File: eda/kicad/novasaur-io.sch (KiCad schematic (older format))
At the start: 77 parts, among them J1 POWER IN, J10 EXPANSION, J11 EXPANSION, J3 AUDIO OUT, J4 KEYBOARD, J5 SERIAL, J5 VIDEO, J6 DISPLAY, J7 AUDIO, J8 EXPANSION, J9 EXPANSION, Q1 2N3904, Q2 2N3904, Q3 2N3904, SW1 POWER, SW2 RESET, U1 74F86, U3 74F11, U38 CD4053, U39 MAX232, U4 74F32, U40 NJM4580, U41 MCP1827S, U42 MCP1700, U6 74F139, U7 74F139

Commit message: add TVS diode ESD protection
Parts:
- removed J7: AUDIO, Connector_PinHeader_2.54mm:PinHeader_1x02_P2.54mm_Vertical, symbol Connector_Generic:Conn_01x02
- added D4, D5, D6: P4KE6.8CA, Diode_THT:D_DO-41_SOD81_P7.62mm_Horizontal, symbol Device:D_TVS_ALT
- C11, C12: value 22u -> 10u
- J3: footprint Connector_Audio:Jack_3.5mm_CUI_SJ1-3533NG_Horizontal -> Connector_Audio:Jack_3.5mm_CUI_SJ1-3533NG_Horizontal_CircularHoles
- J5: value VIDEO -> GPU OUT; footprint Connector_PinHeader_2.54mm:PinHeader_1x06_P2.54mm_Vertical -> Connector_PinSocket_2.54mm:PinSocket_1x08_P2.54mm_Vertical; symbol Connector_Generic:Conn_01x06 -> Connector_Generic:Conn_01x08
- renumbered J11 to J10, J8 to J7, J9 to J8, J10 to J9
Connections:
- net labels added: audio, pwron
- wire segments 332 -> 344
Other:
- moved on the sheet: J10, J4, J7, J8, J9, JP3, R10, R11, R12, R13, R14, R8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

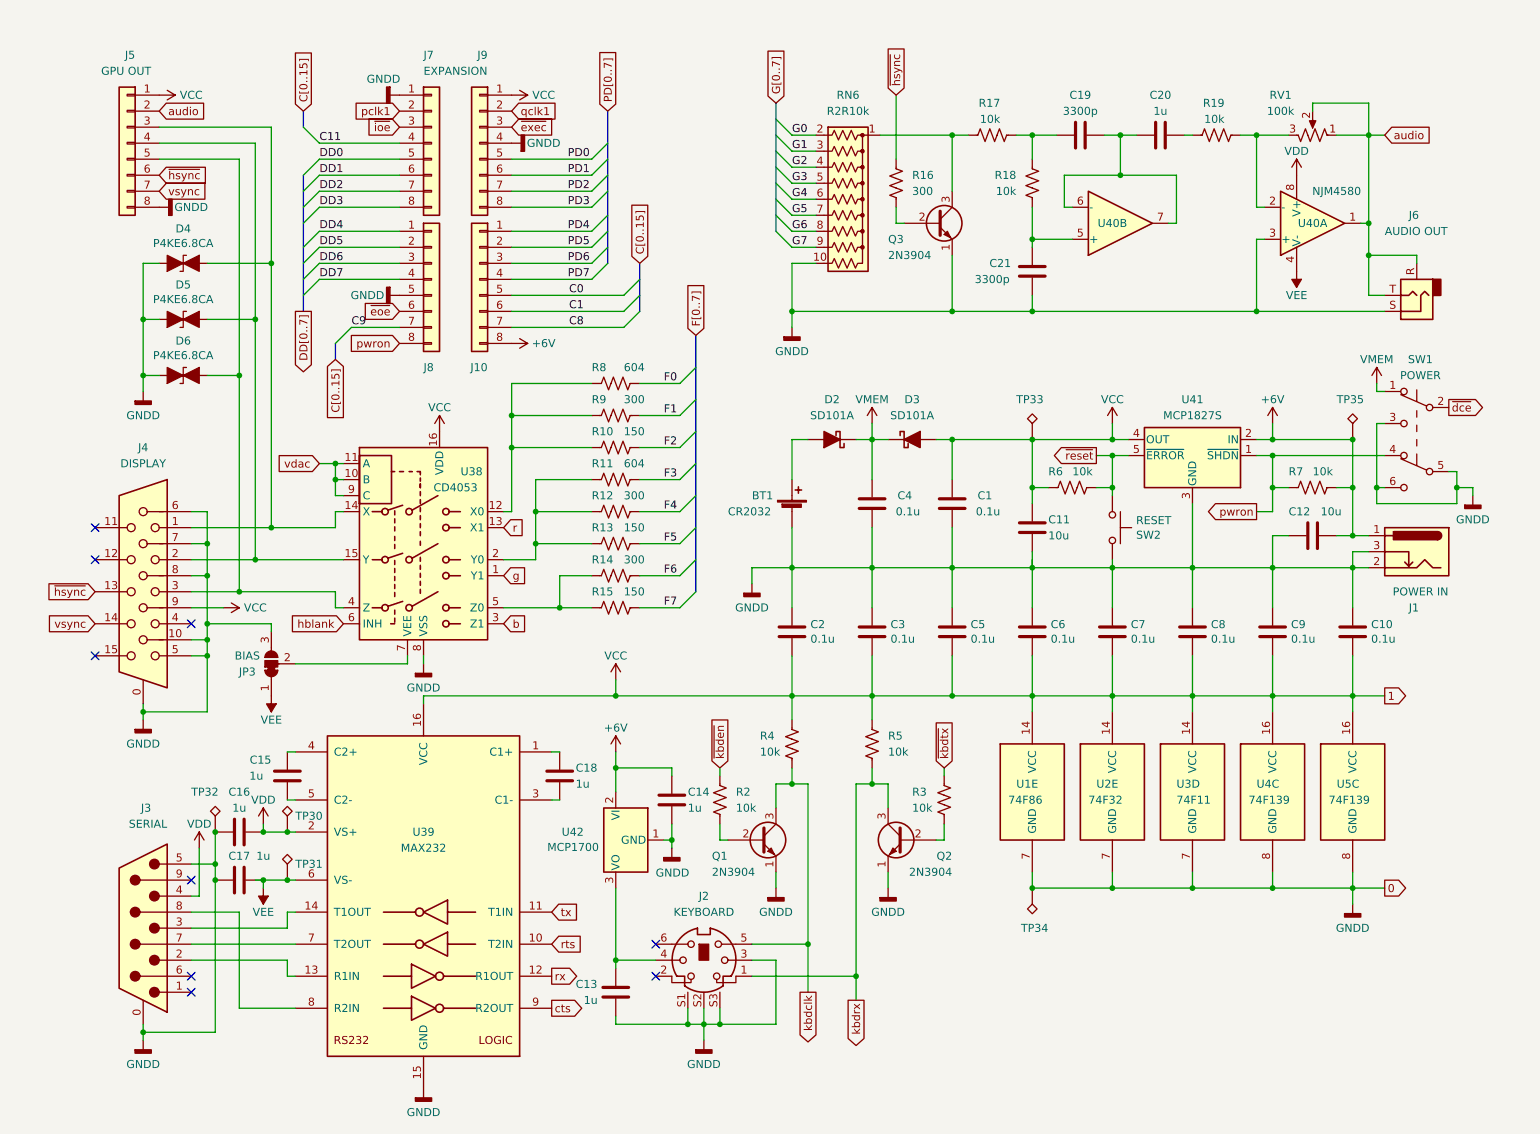
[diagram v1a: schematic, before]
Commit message: remove 6v regulator go back to rev.1 do not collect 00
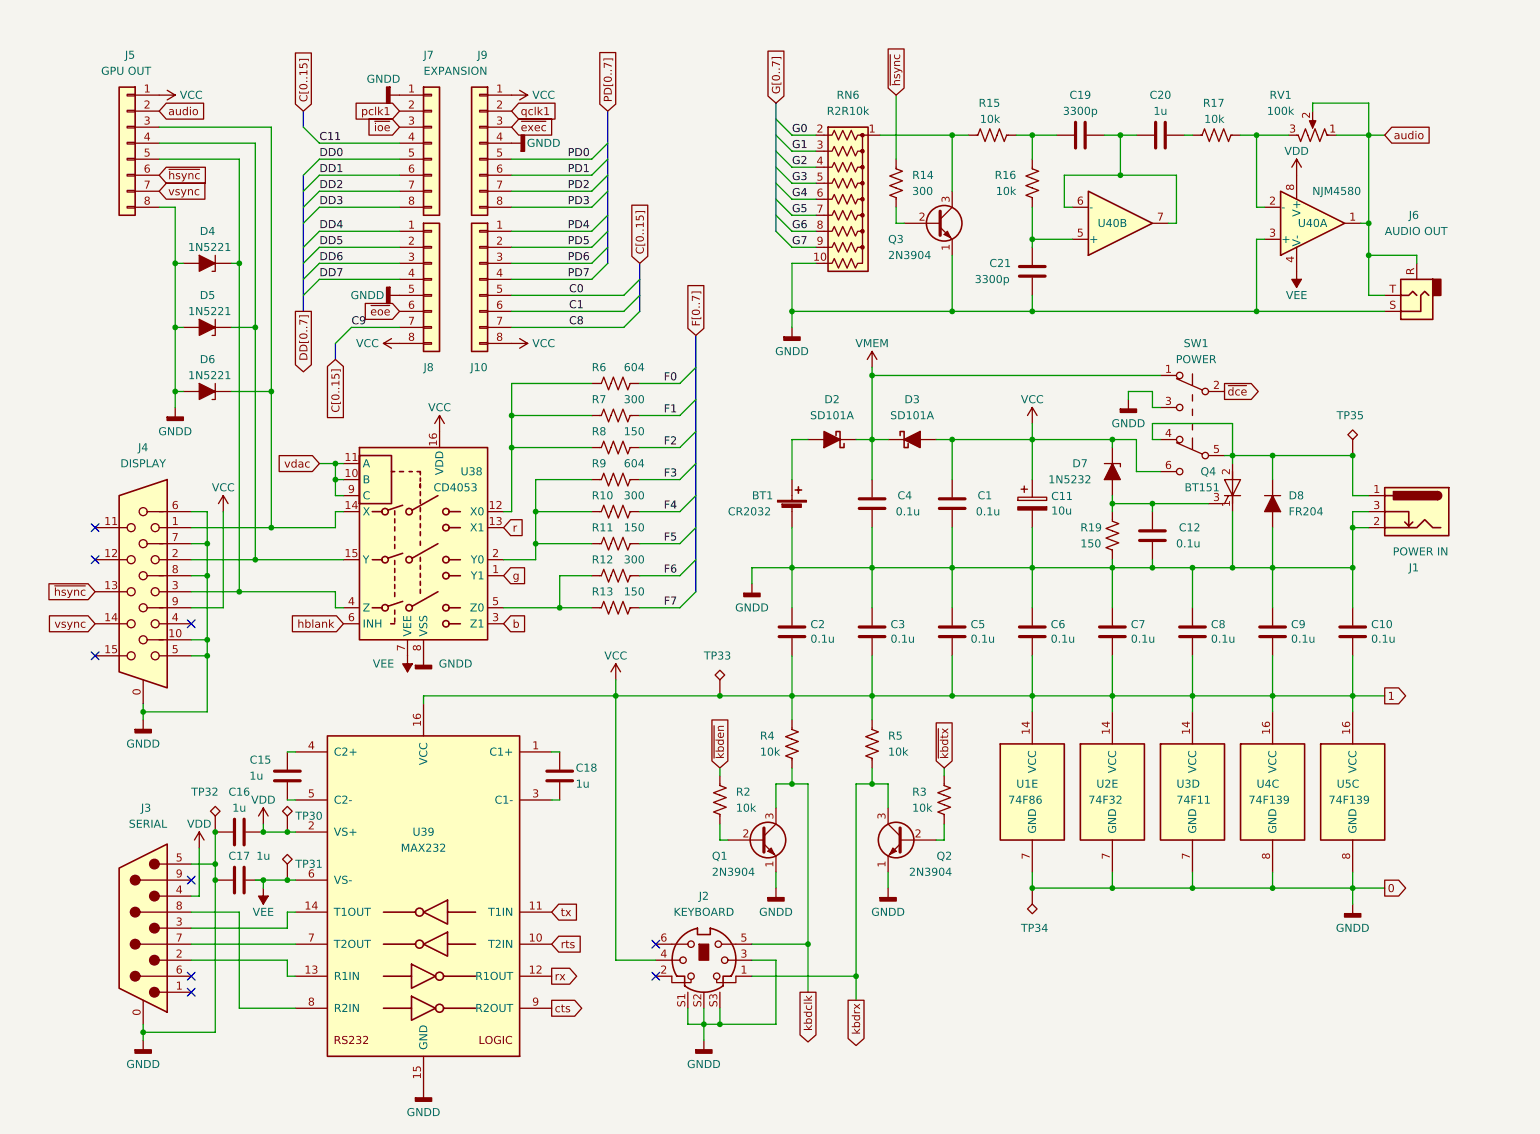
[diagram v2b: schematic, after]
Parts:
- removed C11: 10u, Capacitor_THT:C_Disc_D5.0mm_W2.5mm_P2.50mm, symbol Device:C
- removed C13, C14: 1u, Capacitor_THT:C_Disc_D5.1mm_W3.2mm_P5.00mm, symbol Device:C
- removed D4, D5, D6: P4KE6.8CA, Diode_THT:D_DO-41_SOD81_P7.62mm_Horizontal, symbol Device:D_TVS_ALT
- removed JP3: BIAS, Jumper:SolderJumper-3_P1.3mm_Bridged12_RoundedPad1.0x1.5mm, symbol Jumper:SolderJumper_3_Bridged12
- removed R6, R7: 10k, Resistor_THT:R_Axial_DIN0204_L3.6mm_D1.6mm_P7.62mm_Horizontal, symbol Device:R_US
- removed SW2: RESET, Button_Switch_THT:SW_DIP_SPSTx01_Slide_6.7x4.1mm_W7.62mm_P2.54mm_LowProfile, symbol Switch:SW_Push
- removed U41: MCP1827S, Package_TO_SOT_THT:TO-220-5_P3.4x3.8mm_StaggerOdd_Lead7.13mm_TabDown, symbol Regulator_Linear:LP3963-3.3
- removed U42: MCP1700, Package_TO_SOT_THT:TO-92_HandSolder, symbol Regulator_Linear:MCP1700-5002E_TO92
- added C11: 10u, Capacitor_THT:CP_Radial_Tantal_D5.0mm_P5.00mm, symbol Device:CP
- added D4, D5, D6: 1N5221, Diode_THT:D_DO-35_SOD27_P7.62mm_Horizontal, symbol Device:D_Zener_ALT
- added D7: 1N5232, Diode_THT:D_DO-35_SOD27_P7.62mm_Horizontal, symbol Device:D_Zener_ALT
- added D8: FR204, Diode_THT:D_DO-15_P10.16mm_Horizontal, symbol Device:D_ALT
- added Q4: BT151, Package_TO_SOT_THT:TO-220-3_Vertical, symbol Triac_Thyristor:TIC106
- added R19: 150, Resistor_THT:R_Axial_DIN0204_L3.6mm_D1.6mm_P7.62mm_Horizontal, symbol Device:R_US
- C12: value 10u -> 0.1u; footprint Capacitor_THT:C_Disc_D5.0mm_W2.5mm_P2.50mm -> Capacitor_THT:C_Disc_D5.0mm_W2.5mm_P5.00mm
- TP35: value +6v -> Vin
- renumbered R12 to R10, R13 to R11, R14 to R12, R15 to R13, R16 to R14, R17 to R15, R18 to R16, R19 to R17, R8 to R6, R9 to R7, R10 to R8, R11 to R9
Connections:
- net GNDD: now also C12.1, C11.2, D4.2 (A), D5.2 (A), D6.2 (A), D8.2 (A), Q4.1 (K), R19.2; no longer C12.2, SW1.5 (B), SW1.6 (C)
- net VCC: now also J10.8 (Pin_8), J4.4, J8.8 (Pin_8), SW1.6 (C), C11.1, D7.1 (K)
- net VEE: now also U38.7 (VEE)
- net at J5.3 (Pin_3), J6.1, U38.14 (X): now also D6.1 (K)
- net at J5.4 (Pin_4), J6.2, U38.15 (Y): now also D5.1 (K)
- net at J5.5 (Pin_5), J6.3, U38.4 (Z): now also D4.1 (K)
- net +6V: no longer names the net of J1.1, TP35.1
- net +6V: now also SW1.4 (A), SW1.5 (B), D8.1 (K), Q4.2 (A); no longer C12.1, J10.8 (Pin_8)
- removed net pwron: J8.8 (Pin_8), SW1.4 (A)
- new net: C12.2, D7.2 (A), Q4.3 (G), R19.1
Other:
- moved on the sheet: J1, SW1, TP33, TP35

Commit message: Rev. 10 with 5v PSU
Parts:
- removed D4, D5, D6: 1N5221, Diode_THT:D_DO-35_SOD27_P7.62mm_Horizontal, symbol Device:D_Zener_ALT
- added D4, D5, D6, D7, D8, D9: SD101A, Diode_THT:D_DO-35_SOD27_P7.62mm_Horizontal, symbol Device:D_Schottky_ALT
- C11: value 10u -> 22u
- D11: renamed from D8; footprint Diode_THT:D_DO-15_P10.16mm_Horizontal -> Diode_THT:D_DO-15_P12.70mm_Horizontal
- renumbered D7 to D10
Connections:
- net GNDD: now also J10.8 (Pin_8), D4.2 (A), D5.2 (A), D6.2 (A)
- net VCC: now also D7.1 (K), D8.1 (K), D9.1 (K); no longer J10.8 (Pin_8)
- net at J5.3 (Pin_3), J6.1, U38.14 (X): now also D6.1 (K), D9.2 (A)
- net at J5.4 (Pin_4), J6.2, U38.15 (Y): now also D5.1 (K), D8.2 (A)
- net at J5.5 (Pin_5), J6.3, U38.4 (Z): now also D4.1 (K), D7.2 (A)
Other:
- moved on the sheet: D11, TP34

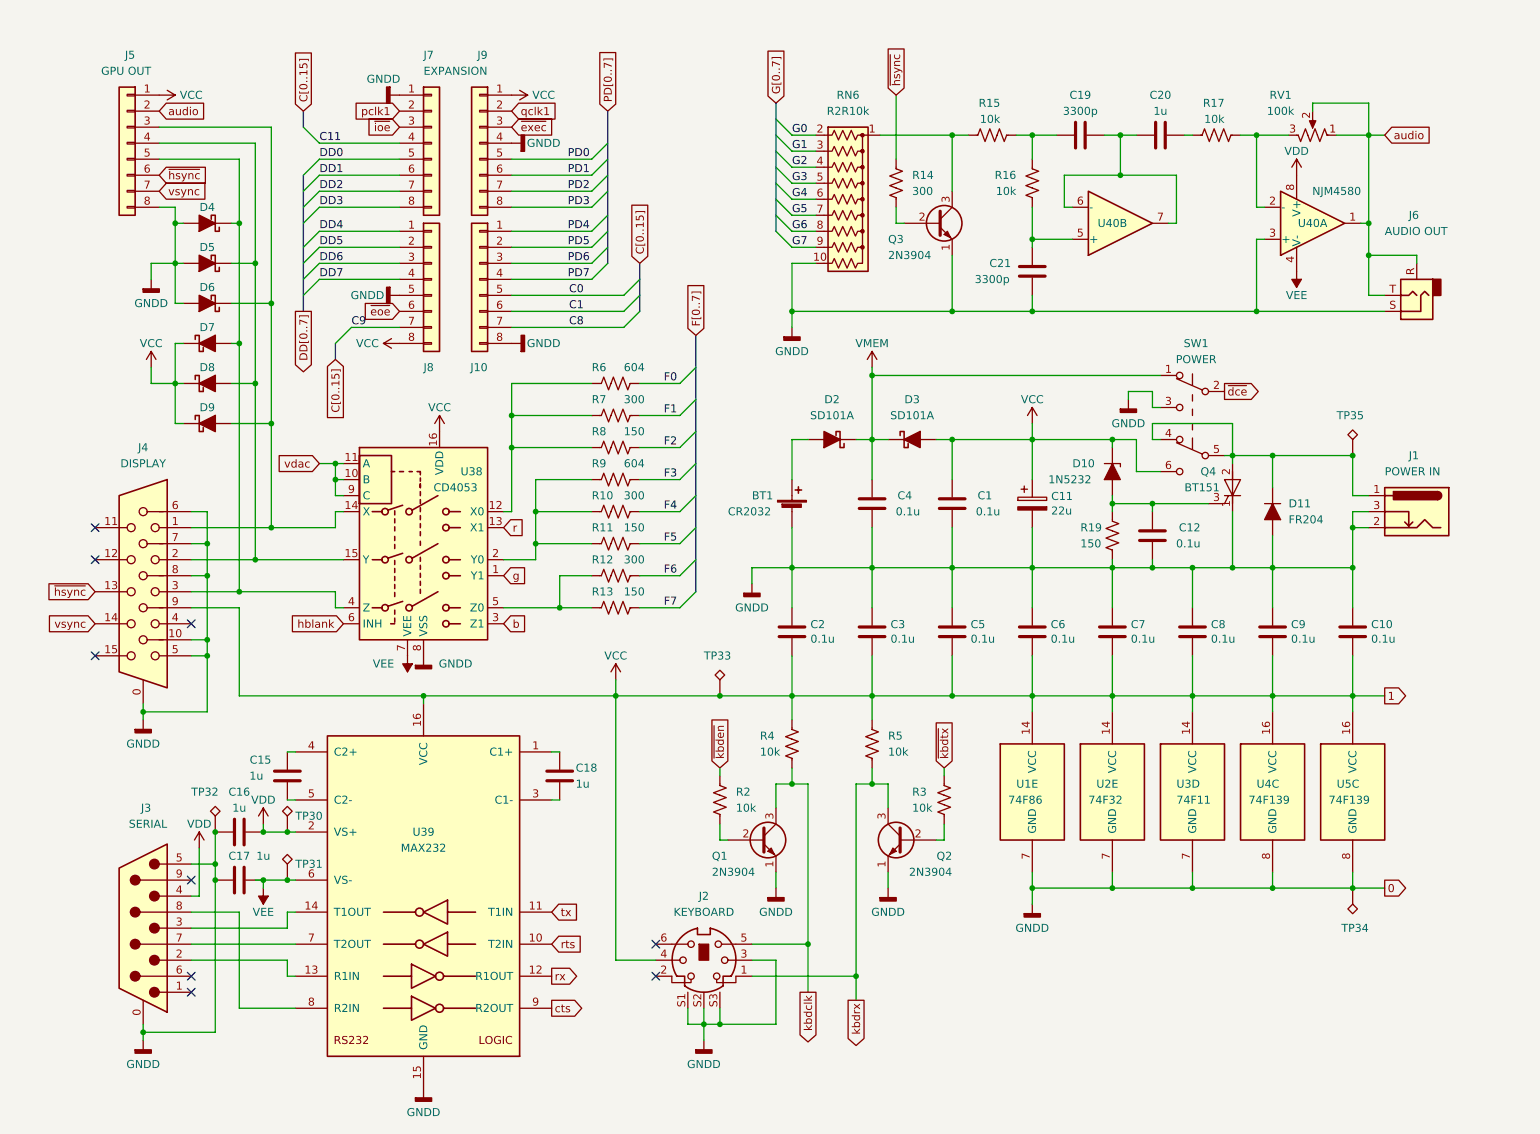
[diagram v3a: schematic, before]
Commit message: remove option for 128k RAM
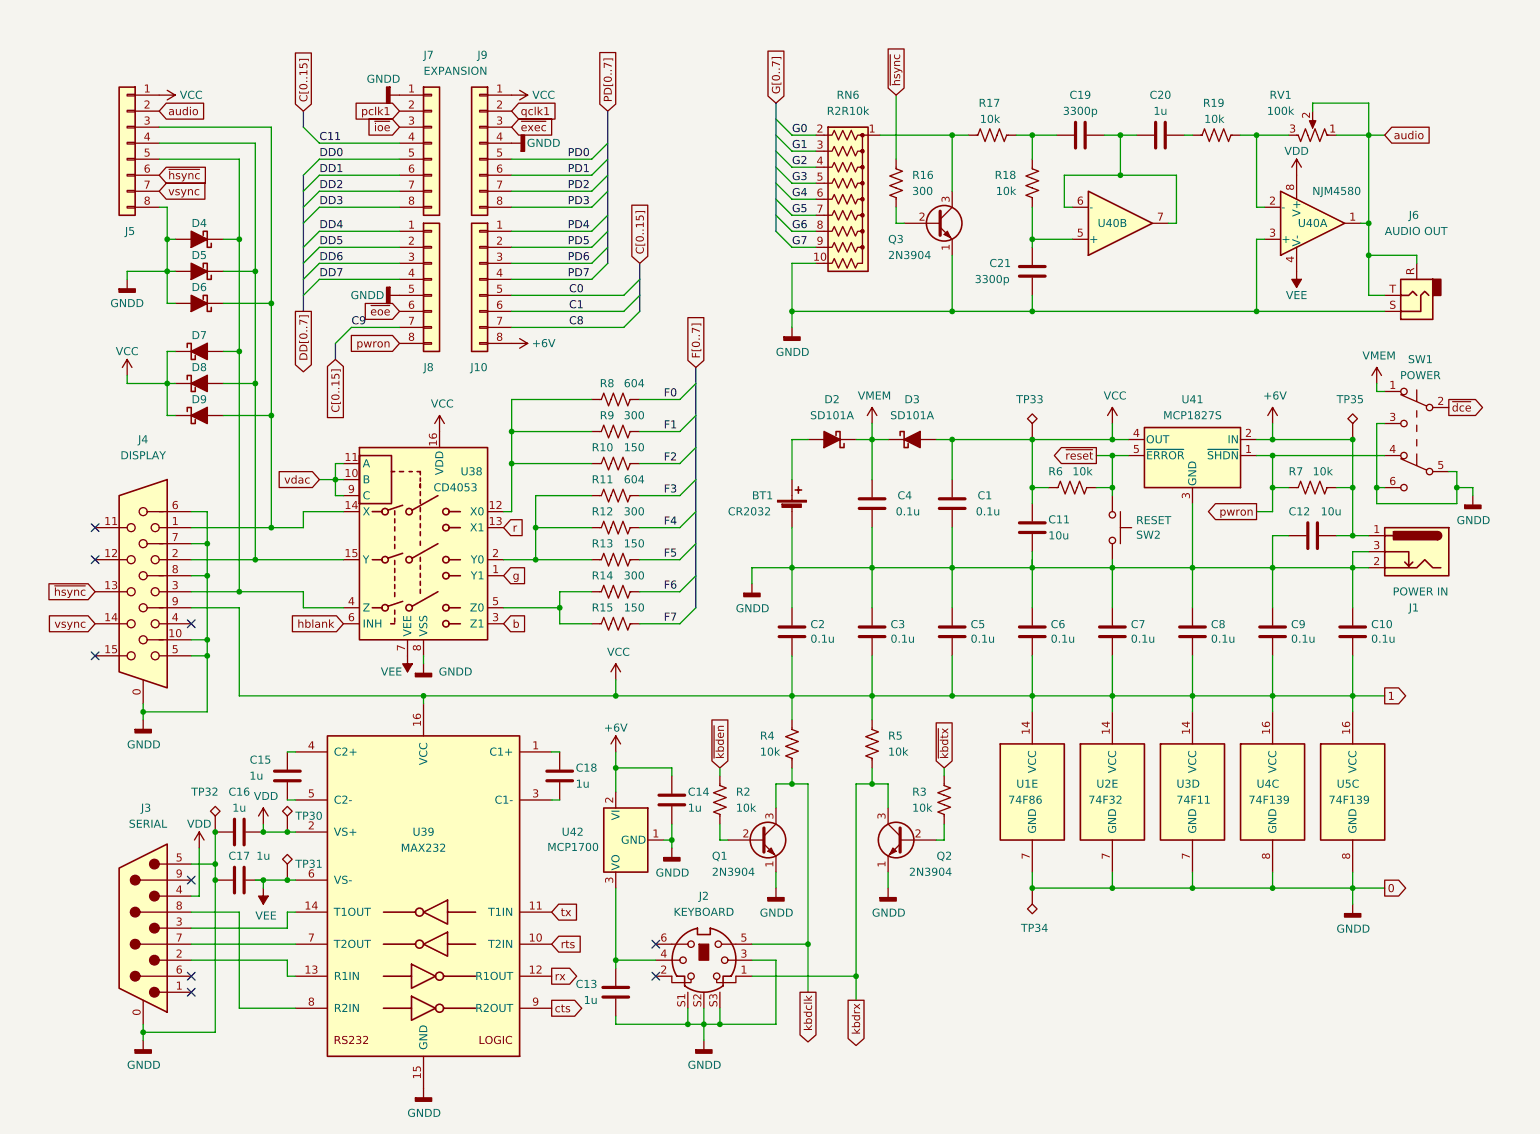
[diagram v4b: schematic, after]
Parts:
- removed C11: 22u, Capacitor_THT:CP_Radial_Tantal_D5.0mm_P5.00mm, symbol Device:CP
- removed D10: 1N5232, Diode_THT:D_DO-35_SOD27_P7.62mm_Horizontal, symbol Device:D_Zener_ALT
- removed D11: FR204, Diode_THT:D_DO-15_P12.70mm_Horizontal, symbol Device:D_ALT
- removed Q4: BT151, Package_TO_SOT_THT:TO-220-3_Vertical, symbol Triac_Thyristor:TIC106
- removed R19: 150, Resistor_THT:R_Axial_DIN0204_L3.6mm_D1.6mm_P7.62mm_Horizontal, symbol Device:R_US
- added C11: 10u, Capacitor_THT:C_Disc_D5.0mm_W2.5mm_P2.50mm, symbol Device:C
- added C13, C14: 1u, Capacitor_THT:C_Disc_D5.1mm_W3.2mm_P5.00mm, symbol Device:C
- added R6, R7: 10k, Resistor_THT:R_Axial_DIN0204_L3.6mm_D1.6mm_P7.62mm_Horizontal, symbol Device:R_US
- added SW2: RESET, Button_Switch_THT:SW_DIP_SPSTx01_Slide_6.7x4.1mm_W7.62mm_P2.54mm_LowProfile, symbol Switch:SW_Push
- added U41: MCP1827S, Package_TO_SOT_THT:TO-220-5_P3.4x3.8mm_StaggerOdd_Lead7.13mm_TabDown, symbol Regulator_Linear:LP3963-3.3
- added U42: MCP1700, Package_TO_SOT_THT:TO-92_HandSolder, symbol Regulator_Linear:MCP1700-5002E_TO92
- C12: value 0.1u -> 10u; footprint Capacitor_THT:C_Disc_D5.0mm_W2.5mm_P5.00mm -> Capacitor_THT:C_Disc_D5.0mm_W2.5mm_P2.50mm
- TP35: value Vin -> +6v
- renumbered R8 to R10, R9 to R11, R10 to R12, R11 to R13, R12 to R14, R13 to R15, R14 to R16, R15 to R17, R16 to R18, R17 to R19, R6 to R8, R7 to R9
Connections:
- net GNDD: now also C12.2, SW1.5 (B), SW1.6 (C), C11.2, C13.2, C14.2, SW2.1, U41.3 (GND), U42.1 (GND); no longer C12.1, J10.8 (Pin_8)
- net VCC: now also C11.1, R6.2, U41.4 (OUT); no longer J4.4, J8.8 (Pin_8), SW1.6 (C)
- net +6V: now reaches J1.1, TP35.1
- net +6V: now also C12.1, J10.8 (Pin_8), C14.1, R7.1, U41.2 (IN), U42.2 (VI); no longer SW1.4 (A), SW1.5 (B)
- new net: C13.1, J4.4, U42.3 (VO)
- new net pwron: J8.8 (Pin_8), R7.2, SW1.4 (A), U41.1 (~SHDN)
- new net ~reset: R6.1, SW2.2, U41.5 (~ERROR)
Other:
- moved on the sheet: J1, R10, R11, R12, R13, R14, R15, R8, R9, SW1, TP33, TP34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
